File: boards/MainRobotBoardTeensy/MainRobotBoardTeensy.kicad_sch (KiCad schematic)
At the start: 122 parts, among them J1 B3B-XH-A, J10 B4B-XH-A, J11 IDC, J12 B4B-XH-A, J13 B5B-XH-A, J14 B5B-XH-A, J2 B3B-XH-A, J3 B3B-XH-A, J4 B3B-XH-A, J5 B3B-XH-A, J6 B3B-XH-A, J7 B3B-XH-A, J8 B3B-XH-A, J9 B3B-XH-A, Q1 MMBT3904LT1G, Q10 MMBT3904LT1G, Q11 MMBT3904LT1G, Q12 MMBT3904LT1G, Q13 MMBT3904LT1G, Q14 MMBT3904LT1G, Q15 MMBT3904LT1G, Q16 MMBT3904LT1G, Q17 MMBT3904LT1G, Q18 MMBT3904LT1G, Q19 MMBT3904LT1G, Q2 MMBT3904LT1G, Q20 MMBT3904LT1G, Q3 MMBT3904LT1G, Q4 MMBT3904LT1G, Q5 MMBT3904LT1G, Q6 MMBT3904LT1G, Q7 MMBT3904LT1G, Q8 MMBT3904LT1G, Q9 MMBT3904LT1G, U1 Teensy4.0, U2 TLC555CDR, U3 SN74HC08DR, U4 SN74HC08DR, U6 SN74HC08DR

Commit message: Update main and leg board
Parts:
- added R54, R55: 10K, Resistor10K:CRCW060310K0FKEA, symbol Device:R_US
- added R56, R57: 47R, Resistor47:RESC1608X55, symbol Device:R_US
- C1: footprint CC0603JRX7R7BB105:CC0603JRX7R7BB105 -> Capacitor1uF:CC0603JRX7R7BB105
- C2: footprint C0402C103J4RACTU:C0402C103J4RACTU -> Capacitor0.01uF:C0402C103J4RACTU
- C3, C4, C5, C6: LCSC C519560 -> C1622
- D1, D2, D3, D4, D5, D6, D7, D8: footprint NCD0603R1:NCD0603R1 -> LedRed:NCD0603R1
- D10, D11, D12, D13, D14, D15, D16, D17, D18, D19, D20, D9: footprint 150080BS75000:150080BS75000_Modified -> LedBlue:150080BS75000_Modified
- Q1, Q10, Q11, Q12, Q13, Q14, Q15, Q16, Q17, Q18, Q19, Q2, Q20, Q3, Q4, Q5, Q6, Q7, Q8, Q9: footprint SMMBT3904LT1G:MMBT3904LT1G -> Transistor:MMBT3904LT1G
- R1: footprint RC0603FR-07360KL:RC0603FR-07360KL -> Resistor360K:RC0603FR-07360KL
- R10, R3, R4, R5, R6, R7, R8, R9: footprint RCG06031K00FKEA:RCG06031K00FKEA -> Resistor1K:RCG06031K00FKEA
- R11, R12, R13, R14, R15, R16, R17, R18, R19, R20, R21, R22: footprint RC0603FR-07150RL:RESC1607X60N -> Resistor150:RESC1607X60N
- R2, R38, R39, R40, R41, R42, R43, R44, R45, R46, R47, R48, R49, R50, R51, R52, R53: footprint CRCW060310K0FKEA:CRCW060310K0FKEA -> Resistor10K:CRCW060310K0FKEA
- R23, R24, R25, R26, R27, R28, R29, R30, R31, R32, R33: LCSC C4264491 -> C114623
- R34, R35, R36, R37: footprint Resistor2.2K:RESC1607X60N -> Resistor2.2K:RC0603FR-072K2L; LCSC C4264491 -> C114662
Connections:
- net LPWM1 is gone; now on net HEADTILT1LPWM: U3.5 (2B)
- net LPWM2 is gone; now on net HEADTILT2LPWM: U3.13 (4B)
- net LPWM3 is gone; now on net TORSOTILT1LPWM: U4.5 (2B)
- net LPWM4 is gone; now on net TORSOTILT2RPWM: U4.10 (3B)
- net PWMEN1 is gone; now on net HEADTILT1EN: Q1.1 (B)
- net PWMEN2 is gone; now on net HEADTILT2EN: Q2.1 (B)
- net PWMEN3 is gone; now on net TORSOTILT1EN: Q3.1 (B)
- net PWMEN4 is gone; now on net TORSOTILT2EN: Q4.1 (B)
- net RPWM1 is gone; now on net HEADTILT1RPWM: U3.2 (1B)
- net RPWM2 is gone; now on net HEADTILT2RPWM: U3.10 (3B)
- net RPWM3 is gone; now on net TORSOTILT1RPWM: U4.2 (1B)
- net RPWM4 is gone; now on net TORSOTILT2LPWM: U4.13 (4B)
- net SERVOGND is gone; now on net GND: J9.3 (Pin_3)
- net SERVOPWR is gone; now on an unnamed net: J9.1 (Pin_1)
- net +3.3V: now also J9.2 (Pin_2), R54.2, R55.2
- net BLINK: no longer U6.4 (2A)
- net CSHEAD: now also R54.1
- net CSTORSO: now also R55.1
- net CURRENT: no longer C3.1
- net HEAD: no longer C4.1
- net HEADPANPUL: now also Q19.1 (B); no longer U6.5 (2B)
- net MISO: now also R57.1; no longer U1.14 (12_MISO_MQSL)
- net SCK: now also R56.1; no longer U1.20 (13_SCK_CRX1_LED)
- net TORSO1: no longer C5.1
- net TORSO2: no longer C6.1
- net at J2.2 (Pin_2), R35.1: now also C4.1
- net at R31.1, R46.1: no longer J9.2 (Pin_2)
- net at J3.2 (Pin_2), R36.1: now also C5.1
- net at J1.2 (Pin_2), R34.1: now also C3.1
- net at J4.2 (Pin_2), R37.1: now also C6.1
- net HEADPANPULBLINK: no longer names the net of U6.6 (2Y)
- net HEADPANPULBLINK: no longer Q19.1 (B)
- net LPWM1BLINK renamed HEADTILT1LPWMBLINK
- net LPWM2BLINK renamed HEADTILT2LPWMBLINK
- net LPWM3BLINK renamed TORSOTILT1LPWMBLINK
- net LPWM4BLINK renamed TORSOTILT2LPWMBLINK
- net TORSOTILT2LPWMBLINK: now also U4.11 (4Y); no longer U4.8 (3Y)
- net RPWM1BLINK renamed HEADTILT1RPWMBLINK
- net RPWM2BLINK renamed HEADTILT2RPWMBLINK
- net RPWM3BLINK renamed TORSOTILT1RPWMBLINK
- net RPWM4BLINK renamed TORSOTILT2RPWMBLINK
- net TORSOTILT2RPWMBLINK: now also U4.8 (3Y); no longer U4.11 (4Y)
- new net: R57.2, U1.14 (12_MISO_MQSL)
- new net: R56.2, U1.20 (13_SCK_CRX1_LED)
- no-connect marks 29 -> 33
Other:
- note added: "HEAD TILT 1"
- note added: "HEAD TILT 1 LPWM"
- note added: "HEAD TILT 1 RPWM"
- note added: "HEAD TILT 2"
- note added: "HEAD TILT 2 LPWM"
- note added: "HEAD TILT 2 RPWM"
- note added: "TORSO TILT 1"
- note added: "TORSO TILT 1 LPWM"
- note added: "TORSO TILT 1 RPWM"
- note added: "TORSO TILT 2"
- note added: "TORSO TILT 2 LPWM"
- note added: "TORSO TILT 2 RPWM"
- note removed: "LPWM 1"
- note removed: "LPWM 2"
- note removed: "LPWM 3"
- note removed: "LPWM 4"
- note removed: "PWM 1"
- note removed: "PWM 2"
- note removed: "PWM 3"
- note removed: "PWM 4"
- note removed: "RPWM 1"
- note removed: "RPWM 2"
- note removed: "RPWM 3"
- note removed: "RPWM 4"
- note removed: "TODO: need envelope?"
- note removed: "TODO: what is the actual layout?"
- moved on the sheet: C6, MH1, MH2, MH3, MH4, R1, R2, R31, R34, R35, R36, R37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

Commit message: Add OLED display, light bar, voltage and current sensors
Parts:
- removed J1: B3B-XH-A, Connector_JST:JST_XH_B3B-XH-A_1x03_P2.50mm_Vertical, symbol Connector_Generic:Conn_01x03
- removed J12: B4B-XH-A, Connector_JST:JST_XH_B4B-XH-A_1x04_P2.50mm_Vertical, symbol Connector_Generic:Conn_01x04
- removed Q1, Q10, Q11, Q12, Q13, Q14, Q15, Q16, Q17, Q18, Q19, Q2, Q20, Q3, Q4, Q5, Q6, Q7, Q8, Q9: MMBT3904LT1G, Transistor:MMBT3904LT1G, symbol MMBT3904LT1G:MMBT3904LT1G
- added C7, C8: 100nF, Capacitor100nF:CC0603KRX7R9BB104, symbol CC0603JRX7R7BB105:CC0603JRX7R7BB105
- added Q1, Q10, Q11, Q12, Q13, Q14, Q15, Q16, Q17, Q18, Q19, Q2, Q20, Q3, Q4, Q5, Q6, Q7, Q8, Q9: AO3400A, AO3400A:AO3400A, symbol AO3400A:AO3400A
- added R100, R101, R102, R103, R104, R105, R106, R107, R98, R99: 150R, Resistor150:RESC1607X60N, symbol Device:R_US
- added R58, R60, R62, R64, R66, R68, R70, R72, R74, R76, R78, R80, R82, R84, R86, R88, R90, R92, R94, R96: 10K, Resistor10K:CRCW060310K0FKEA, symbol Device:R_US
- added R59, R61, R63, R65, R67, R69, R71, R73, R75, R77, R79, R81, R83, R85, R87, R89, R91, R93, R95, R97: 100K, Resistor100K:CRCW0603100KFKEA, symbol Device:R_US
- added U10: KWL-R1025BB, LedBar:KWL-R1025BB, symbol LedBar:KWL-R1025BB
- added U11: SSD1306, SSD1306:SSD1306, symbol SSD1306:SSD1306
- added U5: INA260, INA260:INA260, symbol INA260:INA260
- added U7: ACS37220, ACS37220:ACS37220, symbol ACS37220:ACS37220
- added U8, U9: SN74HC595DR, ShiftRegister:SN74HC595DR, symbol ShiftRegister:SN74HC595DR
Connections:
- net +3.3V: now also C7.2, C8.2, R100.2, R101.2, R102.2, R103.2, R104.2, R105.2, R106.2, R107.2, R98.2, R99.2, U11.1 (VCC), U5.1 (VCC), U7.1 (VCC), U8.10 (SRCLR_N), U8.16 (VCC), U9.10 (SRCLR_N), U9.16 (VCC)
- net GND: now also C7.1, C8.1, Q1.3, Q10.3, Q11.3, Q12.3, Q13.3, Q14.3, Q15.3, Q16.3, Q17.3, Q18.3, Q19.3, Q2.3, Q20.3, Q3.3, Q4.3, Q5.3, Q6.3, Q7.3, Q8.3, Q9.3, R59.2, R61.2, R63.2, R65.2, R67.2, R69.2, R71.2, R73.2, R75.2, R77.2, R79.2, R81.2, R83.2, R85.2, R87.2, R89.2, R91.2, R93.2, R95.2, R97.2, U11.2 (GND), U5.2 (GND), U7.2 (GND), U8.13 (OE_N), U8.8 (GND), U9.13 (OE_N), U9.8 (GND)
- net HEADENCODERST: now also R72.1, R73.1
- net HEADPANDIR: now also R96.1, R97.1
- net HEADPANEN: now also R68.1, R69.1
- net HEADPANPUL: now also R94.1, R95.1
- net HEADTILT1EN: now also R58.1, R59.1
- net HEADTILT1LPWMBLINK: now also R76.1, R77.1
- net HEADTILT1RPWMBLINK: now also R74.1, R75.1
- net HEADTILT2EN: now also R60.1, R61.1
- net HEADTILT2LPWMBLINK: now also R80.1, R81.1
- net HEADTILT2RPWMBLINK: now also R78.1, R79.1
- net SCK: now also U8.11 (SRCLK), U9.11 (SRCLK)
- net SCL: now also U11.3 (SCL), U5.3 (SCL)
- net SDA: now also U11.4 (SDA), U5.4 (SDA)
- net TORSOENCODERST: now also R70.1, R71.1
- net TORSOPANDIR: now also R92.1, R93.1
- net TORSOPANEN: now also R66.1, R67.1
- net TORSOPANPWMBLINK: now also R90.1, R91.1
- net TORSOTILT1EN: now also R62.1, R63.1
- net TORSOTILT1LPWMBLINK: now also R84.1, R85.1
- net TORSOTILT1RPWMBLINK: now also R82.1, R83.1
- net TORSOTILT2EN: now also R64.1, R65.1
- net TORSOTILT2LPWMBLINK: now also R88.1, R89.1
- net TORSOTILT2RPWMBLINK: now also R86.1, R87.1
- net at D2.1 (K): now also Q2.2
- net at D15.1 (K): now also Q15.2
- net at D5.1 (K): now also Q5.2
- net at D17.1 (K): now also Q17.2
- net at C3.1, R34.1: now also U7.3 (VOUT)
- net at D16.1 (K): now also Q16.2
- net at D19.1 (K): now also Q19.2
- net at D11.1 (K): now also Q11.2
- net at D3.1 (K): now also Q3.2
- net at D8.1 (K): now also Q8.2
- net at D13.1 (K): now also Q13.2
- net at D10.1 (K): now also Q10.2
- net at D6.1 (K): now also Q6.2
- net at D20.1 (K): now also Q20.2
- net at D7.1 (K): now also Q7.2
- net MOSI: now reaches U1.13 (11_MOSI_CTX1)
- net MOSI: now also U8.14 (SER)
- net RCLK1: now reaches U1.42 (31_CTX3)
- net RCLK1: now also U8.12 (RCLK)
- net RCLK2: now reaches U1.43 (32_OUT1B)
- net RCLK2: now also U9.12 (RCLK)
- net at D1.1 (K): now also Q1.2
- net at D14.1 (K): now also Q14.2
- net at D18.1 (K): now also Q18.2
- net at D12.1 (K): now also Q12.2
- net at D9.1 (K): now also Q9.2
- net at D4.1 (K): now also Q4.2
- new net: R101.1, U10.14 (LED4+)
- new net: Q5.1, R66.2
- new net: Q10.1, R76.2
- new net: Q7.1, R70.2
- new net: R107.1, U10.20 (LED10+)
- new net: R104.1, U10.17 (LED7+)
- new net: Q17.1, R90.2
- new net: Q13.1, R82.2
- new net: Q8.1, R72.2
- new net: Q12.1, R80.2
- new net: R99.1, U10.12 (LED2+)
- new net: Q16.1, R88.2
- new net: Q18.1, R92.2
- new net: Q1.1, R58.2
- new net: Q2.1, R60.2
- new net: Q20.1, R96.2
- new net: Q15.1, R86.2
- new net: Q9.1, R74.2
- new net: Q14.1, R84.2
- new net: Q11.1, R78.2
- new net: U8.9 (QH'), U9.14 (SER)
- new net: Q4.1, R64.2
- new net: R98.1, U10.11 (LED1+)
- new net: Q19.1, R94.2
- new net: R106.1, U10.19 (LED9+)
- new net: R103.1, U10.16 (LED6+)
- new net: R100.1, U10.13 (LED3+)
- new net: R102.1, U10.15 (LED5+)
- new net: R105.1, U10.18 (LED8+)
- new net: Q3.1, R62.2
- new net: Q6.1, R68.2
- new net LED1: U10.1 (LED1-), U8.15 (QA)
- new net LED10: U10.10 (LED10-), U9.1 (QB)
- new net LED2: U10.2 (LED2-), U8.1 (QB)
- new net LED3: U10.3 (LED3-), U8.2 (QC)
- new net LED4: U10.4 (LED4-), U8.3 (QD)
- new net LED5: U10.5 (LED5-), U8.4 (QE)
- new net LED6: U10.6 (LED6-), U8.5 (QF)
- new net LED7: U10.7 (LED7-), U8.6 (QG)
- new net LED8: U10.8 (LED8-), U8.7 (QH)
- new net LED9: U10.9 (LED9-), U9.15 (QA)
- no-connect marks 33 -> 37
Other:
- note added: "Battery Charge Meter"
- note added: "Current Sensor"
- note added: "Shift Registers"
- note added: "Voltage / Current Meter OLED Display"
- note added: "Voltage Sensor"
- note removed: "CURRENT SENSOR"
- note removed: "VOLTAGE SENSOR"
- moved on the sheet: C1, C2, C3, C4, C5, C6, D1, D10, D11, D12, D13, D14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

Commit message: Finalize main robot board
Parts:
- Q1, Q10, Q11, Q12, Q13, Q14, Q15, Q16, Q17, Q18, Q19, Q2, Q20, Q3, Q4, Q5, Q6, Q7, Q8, Q9: LCSC (none) -> C20917
- U8, U9: LCSC (none) -> C10092
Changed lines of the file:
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@@
 			)
 		)
+		(property "LCSC" "C20917"
+			(at 295.91 242.57 0)
+			(effects
+				(font
+					(size 1.27 1.27)
+				)
+				(hide yes)
+			)
+		)
 		(pin "1"
 		)
@@
 			)
 		)
+		(property "LCSC" "C20917"
+			(at 175.26 269.24 0)
+			(effects
+				(font
+					(size 1.27 1.27)
+				)
+				(hide yes)
+			)
+		)
 		(pin "1"
 		)
@@
 			)
 		)
+		(property "LCSC" "C20917"
+			(at 375.92 215.9 0)
+			(effects
+				(font
+					(size 1.27 1.27)
+				)
+				(hide yes)
+			)
+		)
 		(pin "1"
 		)
@@
 			)
 		)
+		(property "LCSC" "C20917"
+			(at 99.06 214.63 0)
+			(effects
+				(font
+					(size 1.27 1.27)
+				)
+				(hide yes)
+			)
+		)
 		(pin "1"
 		)
@@
 			)
 		)
+		(property "LCSC" "C20917"
+			(at 99.06 241.3 0)
+			(effects
+				(font
+					(size 1.27 1.27)
+				)
+				(hide yes)
+			)
+		)
 		(pin "1"
 		)
@@
 			)
 		)
+		(property "LCSC" "C20917"
+			(at 375.92 270.51 0)
+			(effects
+				(font
+					(size 1.27 1.27)
+				)
+				(hide yes)
+			)
+		)
 		(pin "1"
 		)
@@
 			)
 		)
+		(property "LCSC" "C20917"
+			(at 295.91 298.45 0)
+			(effects
+				(font
+					(size 1.27 1.27)
+				)
+				(hide yes)
+			)
+		)
 		(pin "1"
 		)
@@
 			)
 		)
+		(property "LCSC" "C10092"
+			(at 290.83 335.28 0)
+			(effects
+				(font
+					(size 1.27 1.27)
+				)
+				(hide yes)
+			)
+		)
 		(pin "13"
 		)
@@
 			)
 		)
+		(property "LCSC" "C20917"
+			(at 375.92 242.57 0)
+			(effects
+				(font
+					(size 1.27 1.27)
+				)
+				(hide yes)
+			)
+		)
 		(pin "1"
 		)
@@
 			)
 		)
+		(property "LCSC" "C20917"
+			(at 455.93 215.9 0)
+			(effects
+				(font
+					(size 1.27 1.27)
+				)
+				(hide yes)
+			)
+		)
 		(pin "1"
 		)
@@
 			)
 		)
+		(property "LCSC" "C20917"
+			(at 295.91 215.9 0)
+			(effects
+				(font
+					(size 1.27 1.27)
+				)
+				(hide yes)
+			)
+		)
 		(pin "1"
 		)
@@
 			)
 		)
+		(property "LCSC" "C20917"
+			(at 175.26 297.18 0)
+			(effects
+				(font
+					(size 1.27 1.27)
+				)
+				(hide yes)
+			)
+		)
 		(pin "1"
 		)
@@
 			)
 		)
+		(property "LCSC" "C20917"
+			(at 175.26 214.63 0)
+			(effects
+				(font
+					(size 1.27 1.27)
+				)
+				(hide yes)
+			)
+		)
 		(pin "1"
 		)
@@
 			)
 		)
+		(property "LCSC" "C20917"
+			(at 295.91 270.51 0)
+			(effects
+				(font
+					(size 1.27 1.27)
+				)
+				(hide yes)
+			)
+		)
 		(pin "1"
 		)
@@
 			)
 		)
+		(property "LCSC" "C20917"
+			(at 375.92 298.45 0)
+			(effects
+				(font
+					(size 1.27 1.27)
+				)
+				(hide yes)
+			)
+		)
 		(pin "1"
 		)
@@
 			)
 		)
+		(property "LCSC" "C20917"
+			(at 99.06 297.18 0)
+			(effects
+				(font
+					(size 1.27 1.27)
+				)
+				(hide yes)
+			)
+		)
 		(pin "1"
 		)
@@
 			)
 		)
+		(property "LCSC" "C20917"
+			(at 455.93 270.51 0)
+			(effects
+				(font
+					(size 1.27 1.27)
+				)
+				(hide yes)
+			)
+		)
 		(pin "1"
 		)
@@
 			)
 		)
+		(property "LCSC" "C20917"
+			(at 455.93 242.57 0)
+			(effects
+				(font
+					(size 1.27 1.27)
+				)
+				(hide yes)
+			)
+		)
 		(pin "1"
 		)
@@
 			)
 		)
+		(property "LCSC" "C20917"
+			(at 455.93 298.45 0)
+			(effects
+				(font
+					(size 1.27 1.27)
+				)
+				(hide yes)
+			)
+		)
 		(pin "1"
 		)
@@
 			)
 		)
+		(property "LCSC" "C20917"
+			(at 175.26 241.3 0)
+			(effects
+				(font
+					(size 1.27 1.27)
+				)
+				(hide yes)
+			)
+		)
 		(pin "1"
 		)
@@
 			)
 		)
+		(property "LCSC" "C20917"
+			(at 99.06 269.24 0)
+			(effects
+				(font
+					(size 1.27 1.27)
+				)
+				(hide yes)
+			)
+		)
 		(pin "1"
 		)
@@
 			(effects
 				(font
+					(size 1.27 1.27)
+				)
+				(hide yes)
+			)
+		)
+		(property "LCSC" "C10092"
+			(at 360.68 335.28 0)
+			(effects
+				(font

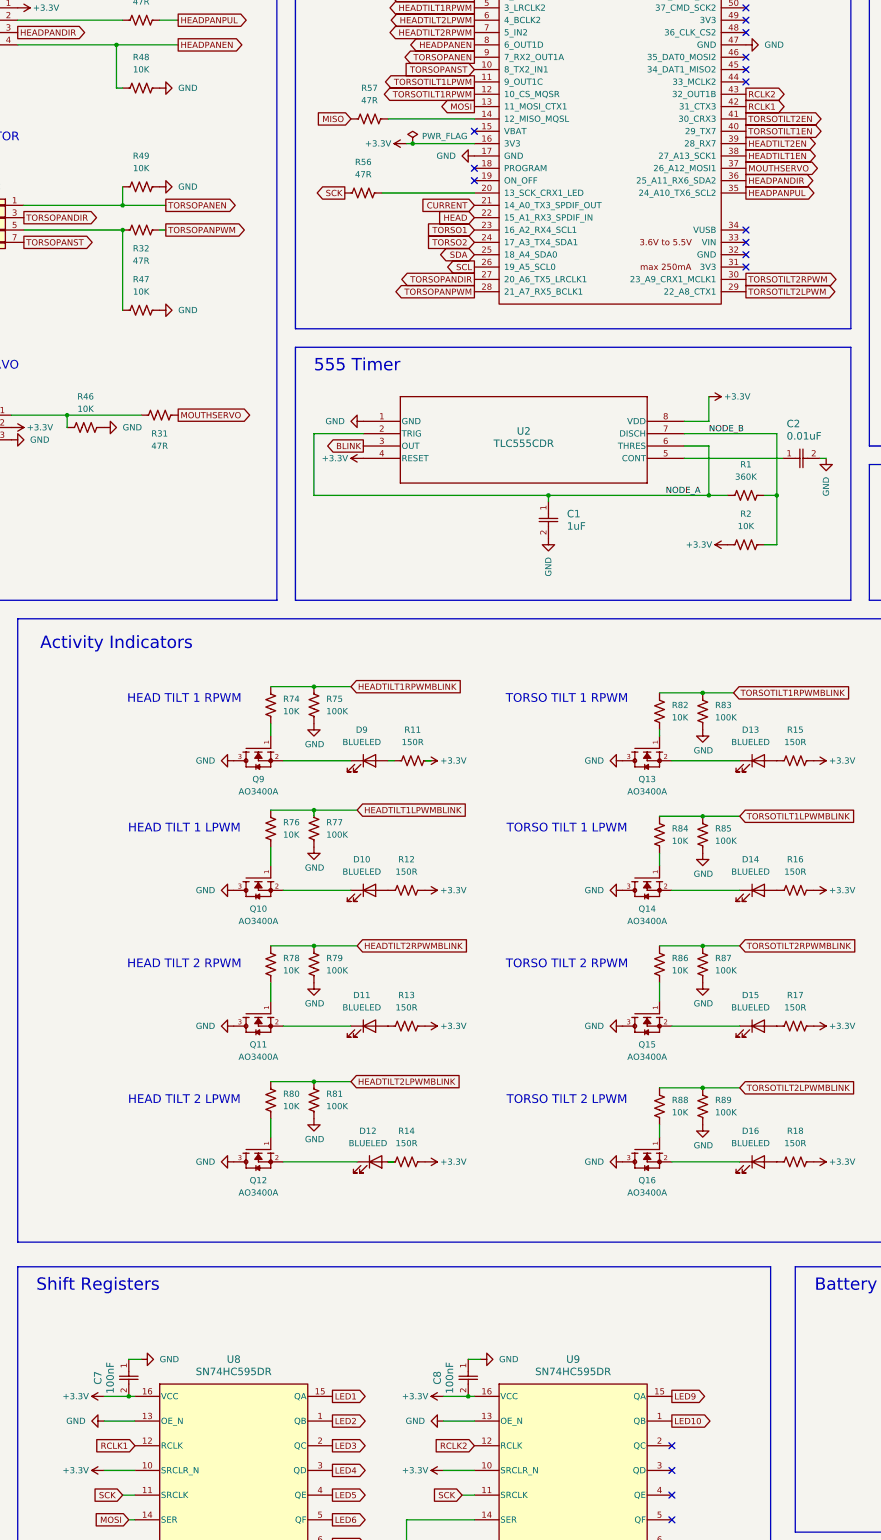
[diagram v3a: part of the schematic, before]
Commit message: Re-routing main board, found a mistake
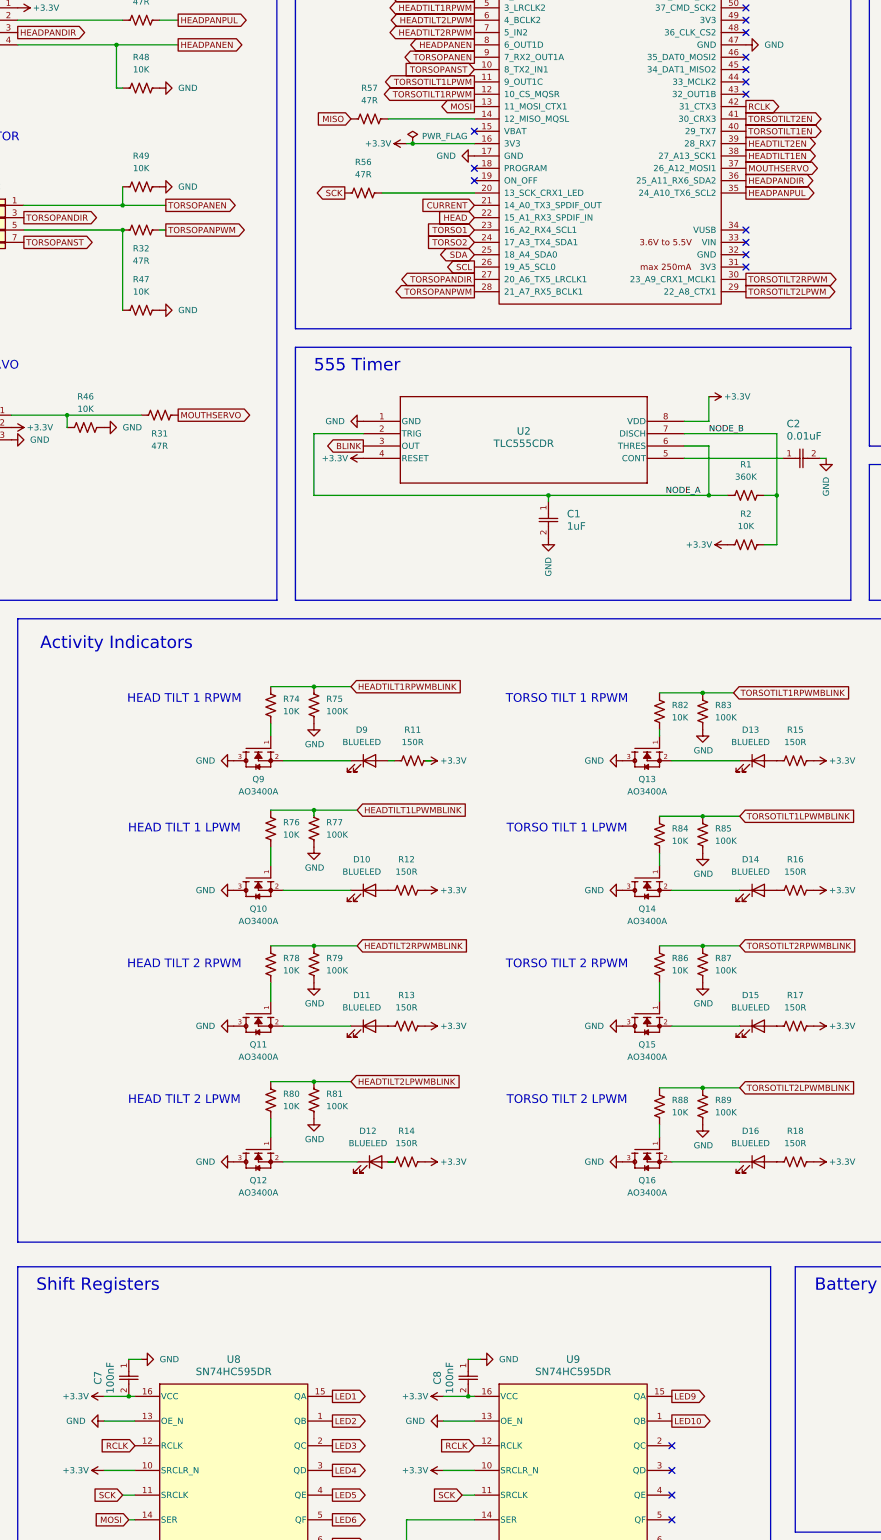
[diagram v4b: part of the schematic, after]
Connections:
- net RCLK1 renamed RCLK
- net RCLK: now also U9.12 (RCLK)
- net RCLK2: no longer names the net of U1.43 (32_OUT1B)
- net RCLK2: no longer U9.12 (RCLK)
- no-connect marks 37 -> 38
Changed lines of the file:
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@@
 	)
 	(no_connect
+		(at 396.24 74.93)
+	)
+	(no_connect
 		(at 487.68 166.37)
 	)
@@
 		)
 	)
-	(global_label "RCLK1"
+	(global_label "RCLK"
 		(shape input)
 		(at 270.51 353.06 180)
@@
 		)
 		(property "Intersheetrefs" "${INTERSHEET_REFS}"
-			(at 261.4772 353.06 0)
+			(at 262.6867 353.06 0)
 			(effects
 				(font
@@
 		)
 	)
-	(global_label "RCLK2"
-		(shape output)
-		(at 396.24 74.93 0)
-		(fields_autoplaced yes)
-		(effects
-			(font
-				(size 1.27 1.27)
-			)
-			(justify left)
-		)
-		(property "Intersheetrefs" "${INTERSHEET_REFS}"
-			(at 405.2728 74.93 0)
-			(effects
-				(font
-					(size 1.27 1.27)
-				)
-				(justify left)
-				(hide yes)
-			)
-		)
-	)
 	(global_label "LED10"
 		(shape output)
@@
 		)
 	)
-	(global_label "RCLK1"
+	(global_label "RCLK"
 		(shape output)
 		(at 396.24 77.47 0)
@@
 		)
 		(property "Intersheetrefs" "${INTERSHEET_REFS}"
-			(at 405.2728 77.47 0)
+			(at 404.0633 77.47 0)
 			(effects
 				(font
@@
 		)
 	)
-	(global_label "RCLK2"
+	(global_label "RCLK"
 		(shape input)
 		(at 340.36 353.06 180)
@@
 		)
 		(property "Intersheetrefs" "${INTERSHEET_REFS}"
-			(at 331.3272 353.06 0)
+			(at 332.5367 353.06 0)
 			(effects
 				(font

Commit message: First draft of main board firmware
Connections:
- net HEADENCODERST: now also U9.3 (QD)
- net TORSOENCODERST: now also U9.2 (QC)
- no-connect marks 38 -> 36
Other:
- moved on the sheet: C4, C5, C6, C7, C8, J13, J2, J3, J4, R35, R36, R37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

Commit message: Finalize main board
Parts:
- removed R59, R61, R63, R65, R67, R69: 100K, Resistor100K:CRCW0603100KFKEA, symbol Device:R_US

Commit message: Add LED number displays to legs board and re-finalize
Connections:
- net GND: now also Q1.2, Q10.2, Q11.2, Q12.2, Q13.2, Q14.2, Q15.2, Q16.2, Q17.2, Q18.2, Q19.2, Q2.2, Q20.2, Q3.2, Q4.2, Q5.2, Q6.2, Q7.2, Q8.2, Q9.2; no longer Q1.3, Q10.3, Q11.3, Q12.3, Q13.3, Q14.3, Q15.3, Q16.3, Q17.3, Q18.3, Q19.3, Q2.3, Q20.3, Q3.3, Q4.3, Q5.3, Q6.3, Q7.3, Q8.3, Q9.3
- net at D10.1 (K): now also Q10.3; no longer Q10.2
- net at D7.1 (K): now also Q7.3; no longer Q7.2
- net at D15.1 (K): now also Q15.3; no longer Q15.2
- net at D13.1 (K): now also Q13.3; no longer Q13.2
- net at D5.1 (K): now also Q5.3; no longer Q5.2
- net at D1.1 (K): now also Q1.3; no longer Q1.2
- net at D19.1 (K): now also Q19.3; no longer Q19.2
- net at D2.1 (K): now also Q2.3; no longer Q2.2
- net at D12.1 (K): now also Q12.3; no longer Q12.2
- net at D8.1 (K): now also Q8.3; no longer Q8.2
- net at D14.1 (K): now also Q14.3; no longer Q14.2
- net at D17.1 (K): now also Q17.3; no longer Q17.2
- net at D9.1 (K): now also Q9.3; no longer Q9.2
- net at D6.1 (K): now also Q6.3; no longer Q6.2
- net at D20.1 (K): now also Q20.3; no longer Q20.2
- net at D11.1 (K): now also Q11.3; no longer Q11.2
- net at D3.1 (K): now also Q3.3; no longer Q3.2
- net at D16.1 (K): now also Q16.3; no longer Q16.2
- net at D4.1 (K): now also Q4.3; no longer Q4.2
- net at D18.1 (K): now also Q18.3; no longer Q18.2
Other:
- moved on the sheet: Q1, Q10, Q11, Q12, Q13, Q14, Q15, Q16, Q17, Q18, Q19, Q2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

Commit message: Main robot board preflight
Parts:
- C2: value 0.01uF -> 10nF; LCSC C2167451 -> C152817
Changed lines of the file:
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@@
 			)
 		)
-		(property "Value" "0.01uF"
+		(property "Value" "10nF"
 			(at 404.622 145.288 0)
 			(effects
@@
 			)
 		)
-		(property "LCSC" "C2167451"
+		(property "LCSC" "C152817"
 			(at 404.622 142.748 0)
 			(effects
